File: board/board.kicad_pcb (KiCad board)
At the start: 2 copper layers, 36.5 x 17.5 mm, 41 parts, among them J2 Conn_01x10, J3 Conn_01x06, J4 Conn_01x02, J7 Conn_01x30, J8 USB_C_Receptacle_USB2.0_16P, J9 Conn_01x02, U2 nPM1300-QEAA, U3 MDBT50Q-P1MV2, U4 TVS_Array, Y1 32k Hz

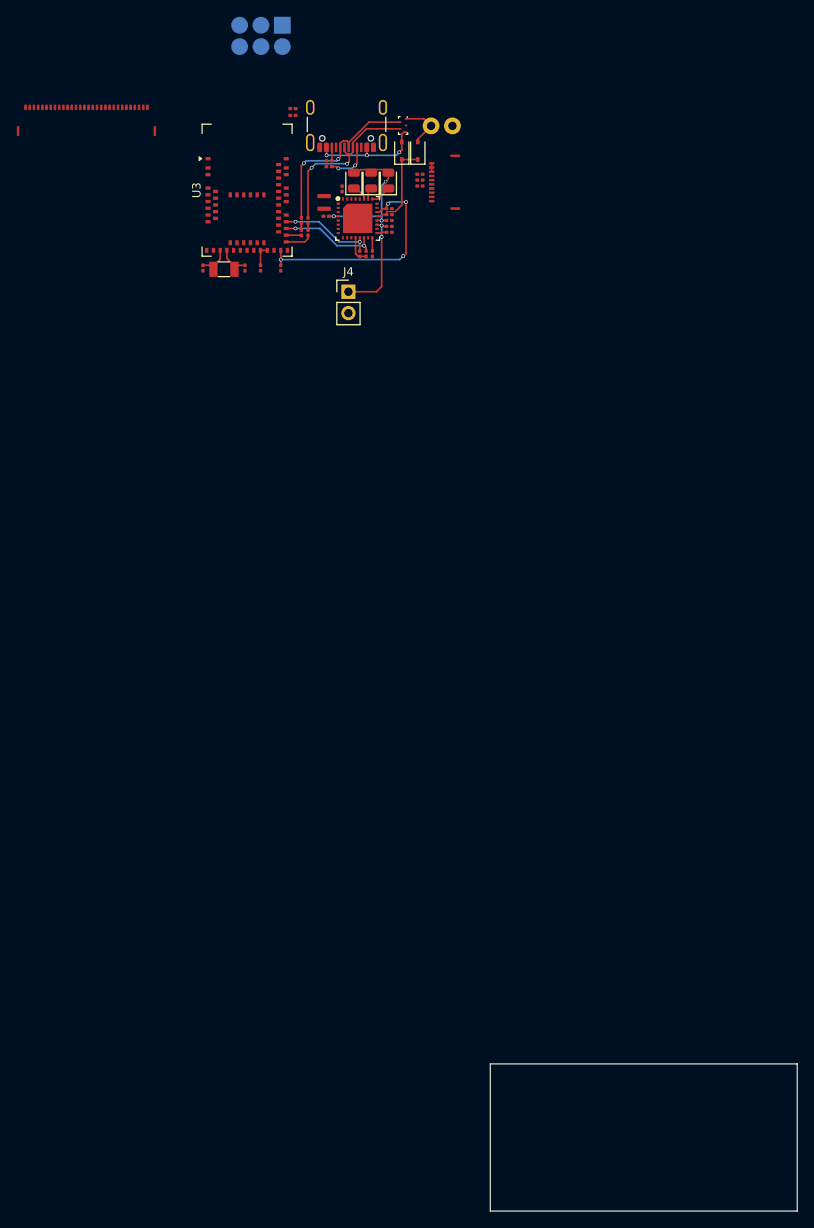
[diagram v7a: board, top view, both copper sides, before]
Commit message: board: pcb route pmic buck converter
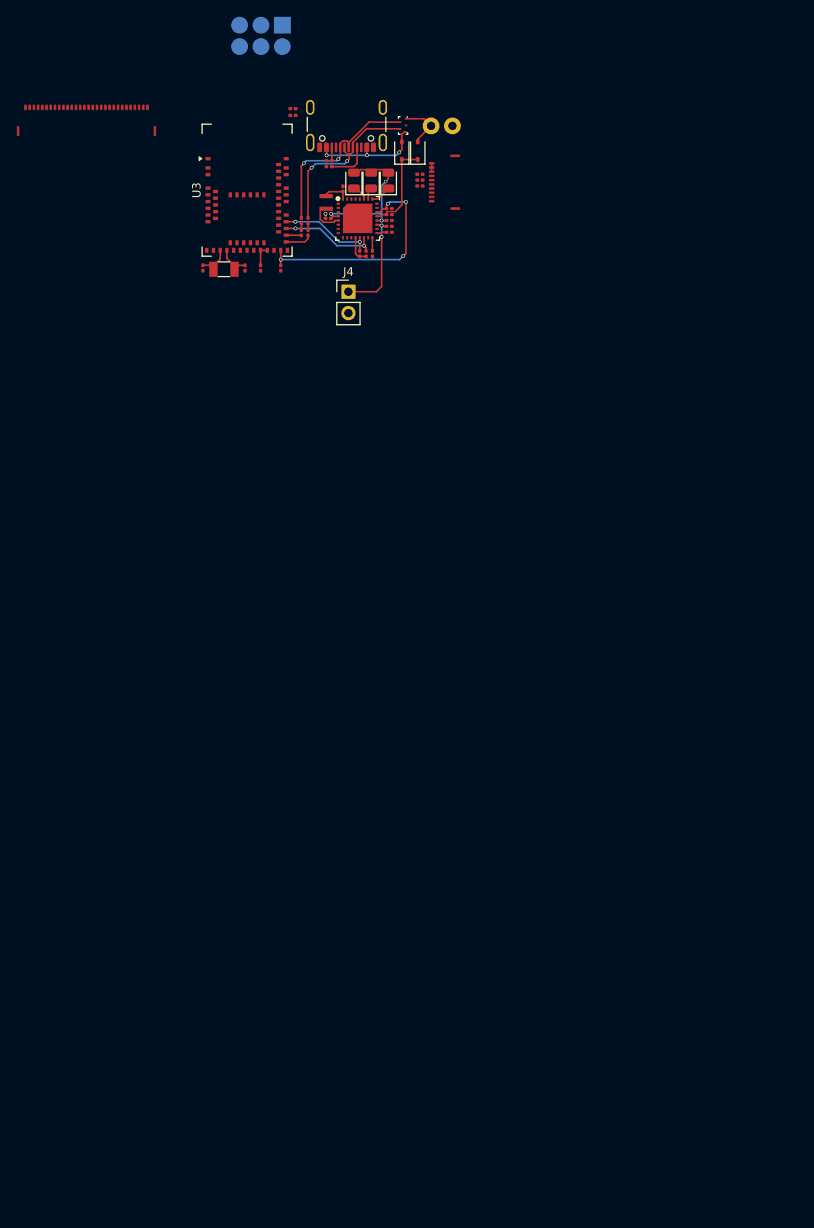
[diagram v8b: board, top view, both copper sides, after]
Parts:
- moved C16 0.35 mm to (109.5, 61.3)
- moved L1 0.25 mm to (109.2, 59.4)
- moved C17 0.10 mm to (111.2, 57.8)
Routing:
- net Net-(U2-SW2): track 0.00 -> 3.43 mm
- net +3V3: track 5.87 -> 9.22 mm
- net GND: track 1.00 -> 1.56 mm, vias 0 -> 1
- net vsys: track 18.1 -> 18.6 mm
- net Net-(J8-CC1): track 5.37 -> 5.08 mm, vias 2 -> 0
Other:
- board outline removed
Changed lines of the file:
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@@
 	(footprint "Capacitor_SMD:C_0201_0603Metric"
 		(layer "F.Cu")
-		(at 109.255 61.05 180)
+		(at 109.5 61.3 180)
 		(descr "Capacitor SMD 0201 (0603 Metric), square (rectangular) end terminal, IPC-7351 nominal, (Body size source: https://www.vishay.com/docs/20052/crcw0201e3.pdf), generated with kicad-footprint-generator")
 		(tags "capacitor")
@@
 	(footprint "Capacitor_SMD:C_0201_0603Metric"
 		(layer "F.Cu")
-		(at 111.15 57.795 90)
+		(at 111.25 57.805 90)
 		(descr "Capacitor SMD 0201 (0603 Metric), square (rectangular) end terminal, IPC-7351 nominal, (Body size source: https://www.vishay.com/docs/20052/crcw0201e3.pdf), generated with kicad-footprint-generator")
 		(tags "capacitor")
@@
 		)
 		(fp_text user "${REFERENCE}"
-			(at 0.895 0 180)
+			(at 0.905 -0.1 180)
 			(layer "F.Fab")
 			(effects
@@
 	(footprint "phiboard:L_0806_2016Metric"
 		(layer "F.Cu")
-		(at 109 59.4 90)
+		(at 109.25 59.4 90)
 		(property "Reference" "L1"
 			(at 0 -1.5 90)
@@
 		(embedded_fonts no)
 	)
-	(gr_rect
-		(start 128.775 161.85)
-		(end 165.275 179.35)
-		(stroke
-			(width 0.05)
-			(type solid)
-		)
-		(fill no)
-		(layer "Edge.Cuts")
-	)
-	(gr_rect
-		(start 130.275 163.6)
-		(end 162.275 177.6)
-		(stroke
-			(width 0.1)
-			(type solid)
-		)
-		(fill no)
-		(layer "User.2")
-	)
 	(gr_line
 		(start 82.3 145.4)
@@
 	)
 	(segment
+		(start 109.85 60.825)
+		(end 110.075 61.05)
+		(width 0.2)
+		(layer "F.Cu")
+		(net 6)
+	)
+	(segment
 		(start 116.425 61.55)
 		(end 115.85 61.55)
@@
 	)
 	(segment
+		(start 110.075 61.05)
+		(end 110.7 61.05)
+		(width 0.2)
+		(layer "F.Cu")
+		(net 6)
+	)
+	(segment
 		(start 112.9875 55.8625)
 		(end 113.35 55.5)
@@
 	)
 	(segment
+		(start 109.85 60.75)
+		(end 109.85 60.825)
+		(width 0.2)
+		(layer "F.Cu")
+		(net 6)
+	)
+	(segment
 		(start 113.35 55.5)
 		(end 116.2875 55.5)
@@
 	)
 	(segment
-		(start 110.15 61.05)
-		(end 109.575 61.05)
-		(width 0.2)
-		(layer "F.Cu")
-		(net 6)
-	)
-	(segment
-		(start 110.15 61.05)
-		(end 110.7 61.05)
+		(start 109.825 61.3)
+		(end 110.075 61.05)
 		(width 0.2)
 		(layer "F.Cu")
@@
 	)
 	(via
-		(at 110.15 61.05)
+		(at 115.85 61.55)
 		(size 0.45)
 		(drill 0.3)
@@
 	)
 	(via
-		(at 115.85 61.55)
+		(at 109.85 60.75)
 		(size 0.45)
 		(drill 0.3)
@@
 	)
 	(segment
-		(start 115.85 61.05)
-		(end 110.15 61.05)
+		(start 115.85 60.75)
+		(end 115.85 61.55)
 		(width 0.2)
 		(layer "B.Cu")
@@
 	(segment
 		(start 115.85 57.4)
-		(end 115.85 61.05)
+		(end 115.85 60.75)
 		(width 0.2)
 		(layer "B.Cu")
@@
 	)
 	(segment
-		(start 115.85 61.55)
-		(end 115.85 61.05)
+		(start 109.85 60.75)
+		(end 115.85 60.75)
 		(width 0.2)
 		(layer "B.Cu")
@@
 	)
 	(segment
+		(start 110.35 61.55)
+		(end 110.15 61.75)
+		(width 0.2)
+		(layer "F.Cu")
+		(net 10)
+	)
+	(segment
+		(start 110.15 61.75)
+		(end 108.9 61.75)
+		(width 0.2)
+		(layer "F.Cu")
+		(net 10)
+	)
+	(segment
+		(start 108.9 61.75)
+		(end 108.55 61.4)
+		(width 0.2)
+		(layer "F.Cu")
+		(net 10)
+	)
+	(segment
+		(start 110.7 61.55)
+		(end 110.35 61.55)
+		(width 0.2)
+		(layer "F.Cu")
+		(net 10)
+	)
+	(segment
+		(start 108.55 61.4)
+		(end 108.55 60.35)
+		(width 0.2)
+		(layer "F.Cu")
+		(net 10)
+	)
+	(segment
 		(start 107.1 62.685)
 		(end 107.1 61.875)
@@
 	)
 	(segment
-		(start 111.75 54.8)
-		(end 112 54.55)
-		(width 0.2)
-		(layer "F.Cu")
-		(net 13)
-	)
-	(segment
 		(start 107.525 55.275)
 		(end 107.1 55.7)
@@
 	)
 	(segment
-		(start 112 54.55)
-		(end 112 53.631)
+		(start 111.43 52.855)
+		(end 111.43 53.322402)
 		(width 0.2)
 		(layer "F.Cu")
@@
 	)
 	(segment
-		(start 111.43 52.855)
-		(end 111.43 53.322402)
+		(start 112.228999 53.631)
+		(end 112.43 53.429999)
 		(width 0.2)
 		(layer "F.Cu")
@@
 	)
 	(segment
-		(start 112.228999 53.631)
-		(end 112.43 53.429999)
+		(start 112 54.25)
+		(end 112 53.631)
 		(width 0.2)
 		(layer "F.Cu")
@@
 	)
 	(segment
+		(start 111.75 54.5)
+		(end 112 54.25)
+		(width 0.2)
+		(layer "F.Cu")
+		(net 13)
+	)
+	(segment
 		(start 112.43 53.429999)
 		(end 112.43 52.855)
@@
 	)
 	(via
-		(at 111.75 54.8)
+		(at 111.75 54.5)
 		(size 0.45)
 		(drill 0.3)
@@
 	)
 	(segment
+		(start 111.45 54.8)
+		(end 108 54.8)
+		(width 0.2)
+		(layer "B.Cu")
+		(net 13)
+	)
+	(segment
 		(start 108 54.8)
-		(end 111.75 54.8)
+		(end 107.525 55.275)
 		(width 0.2)
 		(layer "B.Cu")
@@
 	)
 	(segment
-		(start 107.525 55.275)
-		(end 108 54.8)
+		(start 111.75 54.5)
+		(end 111.45 54.8)
 		(width 0.2)
 		(layer "B.Cu")
@@
 	)
 	(segment
+		(start 109.185 61.3)
+		(end 109.185 60.785)
+		(width 0.2)
+		(layer "F.Cu")
+		(net 45)
+	)
+	(segment
+		(start 109.185 60.785)
+		(end 109.15 60.75)
+		(width 0.2)
+		(layer "F.Cu")
+		(net 45)
+	)
+	(segment
 		(start 121.8 54.75)
 		(end 121.8 55.75)
@@
 		(net 45)
 	)
+	(via
+		(at 109.18 60.75)
+		(size 0.45)
+		(drill 0.3)
+		(layers "F.Cu" "B.Cu")
+		(net 45)
+	)
+	(segment
+		(start 111.25 59)
+		(end 111.25 58.125)
+		(width 0.2)
+		(layer "F.Cu")
+		(net 46)
+	)
+	(segment
+		(start 109.575 58.125)
+		(end 109.25 58.45)
+		(width 0.2)
+		(layer "F.Cu")
+		(net 46)
+	)
+	(segment
+		(start 109.25 58.45)
+		(end 109.25 58.65)
+		(width 0.2)
+		(layer "F.Cu")
+		(net 46)
+	)
+	(segment
+		(start 111.25 58.215)
+		(end 111.15 58.115)
+		(width 0.2)
+		(layer "F.Cu")
+		(net 46)
+	)
 	(segment
 		(start 113.050001 65.815)
@@
 	)
 	(segment
+		(start 111.25 58.125)
+		(end 109.575 58.125)
+		(width 0.2)
+		(layer "F.Cu")
+		(net 46)
+	)
+	(segment
 		(start 101.45 65.1)
 		(end 101.45 66.88)
@@
 	)
 	(segment
-		(start 112.93 54.77)
-		(end 112.7 55)
+		(start 112.55 55.15)
+		(end 112.93 54.77)
 		(width 0.2)
 		(layer "F.Cu")
@@
 	(segment
 		(start 109.92 55.15)
-		(end 110.5 55.15)
+		(end 112.55 55.15)
 		(width 0.2)
 		(layer "F.Cu")
@@
 	)
 	(segment
-		(start 110.5 55.15)
-		(end 110.7 55.35)
-		(width 0.2)
-		(layer "F.Cu")
-		(net 74)
-	)
-	(segment
-		(start 110.7 55.4)
-		(end 110.7 55.3)
-		(width 0.2)
-		(layer "F.Cu")
-		(net 74)
-	)
-	(segment
-		(start 112.93 52.855)
-		(end 112.93 54.77)
+		(start 112.93 54.77)
+		(end 112.93 52.855)
 		(width 0.2)
 		(layer "F.Cu")
 		(net 74)
 	)
-	(via
-		(at 112.7 55)
-		(size 0.45)
-		(drill 0.3)
-		(layers "F.Cu" "B.Cu")
-		(net 74)
-	)
-	(via
-		(at 110.7 55.35)
-		(size 0.45)
-		(drill 0.3)
-		(layers "F.Cu" "B.Cu")
-		(net 74)
-	)
-	(segment
-		(start 110.7 55.35)
-		(end 112.35 55.35)
-		(width 0.2)
-		(layer "B.Cu")
-		(net 74)
-	)
-	(segment
-		(start 112.35 55.35)
-		(end 112.7 55)
-		(width 0.2)
-		(layer "B.Cu")
-		(net 74)
-	)
-	(segment
-		(start 110.7 55.4)
-		(end 110.7 55.425)
-		(width 0.2)
-		(layer "B.Cu")
-		(net 74)
-	)
